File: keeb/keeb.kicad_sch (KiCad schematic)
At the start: 162 parts, among them J101 AVR-ISP-6, J102 USB_C_Receptacle_USB2.0, SW101 SW_Push, SW102 SW_Push, SW103 SW_Push, SW104 SW_Push, SW105 SW_Push, SW106 SW_Push, SW107 SW_Push, SW108 SW_Push, SW109 SW_Push, SW110 SW_Push, SW111 SW_Push, SW112 SW_Push, SW113 SW_Push, SW114 SW_Push, SW115 SW_Push, SW116 SW_Push, SW117 SW_Push, SW118 SW_Push, SW119 SW_Push, SW120 SW_Push, SW121 SW_Push, SW122 SW_Push, SW123 SW_Push, SW124 SW_Push, SW125 SW_Push, SW126 SW_Push, SW127 SW_Push, SW128 SW_Push, SW129 SW_Push, SW130 SW_Push, SW131 SW_Push, SW132 SW_Push, SW133 SW_Push, SW134 SW_Push, SW135 SW_Push, SW136 SW_Push, SW137 SW_Push, SW138 SW_Push, SW139 SW_Push, SW140 SW_Push, SW141 SW_Push, SW142 SW_Push, SW143 SW_Push, SW144 SW_Push, SW145 SW_Push, SW146 SW_Push, SW147 SW_Push, SW148 SW_Push, SW149 SW_Push, SW150 SW_Push, SW151 SW_Push, SW152 SW_Push, SW153 SW_Push, SW154 SW_Push, SW155 SW_Push, SW156 SW_Push, SW157 SW_Push, SW158 SW_Push, SW159 SW_Push, SW160 SW_Push, SW161 SW_Push, SW162 SW_Push, SW163 SW_Push, SW164 SW_Push, SW165 SW_Push, SW166 SW_Push, SW167 SW_Push, U101 TPD2S017, U102 ATmega32U4-MU, Y101 16Mhz

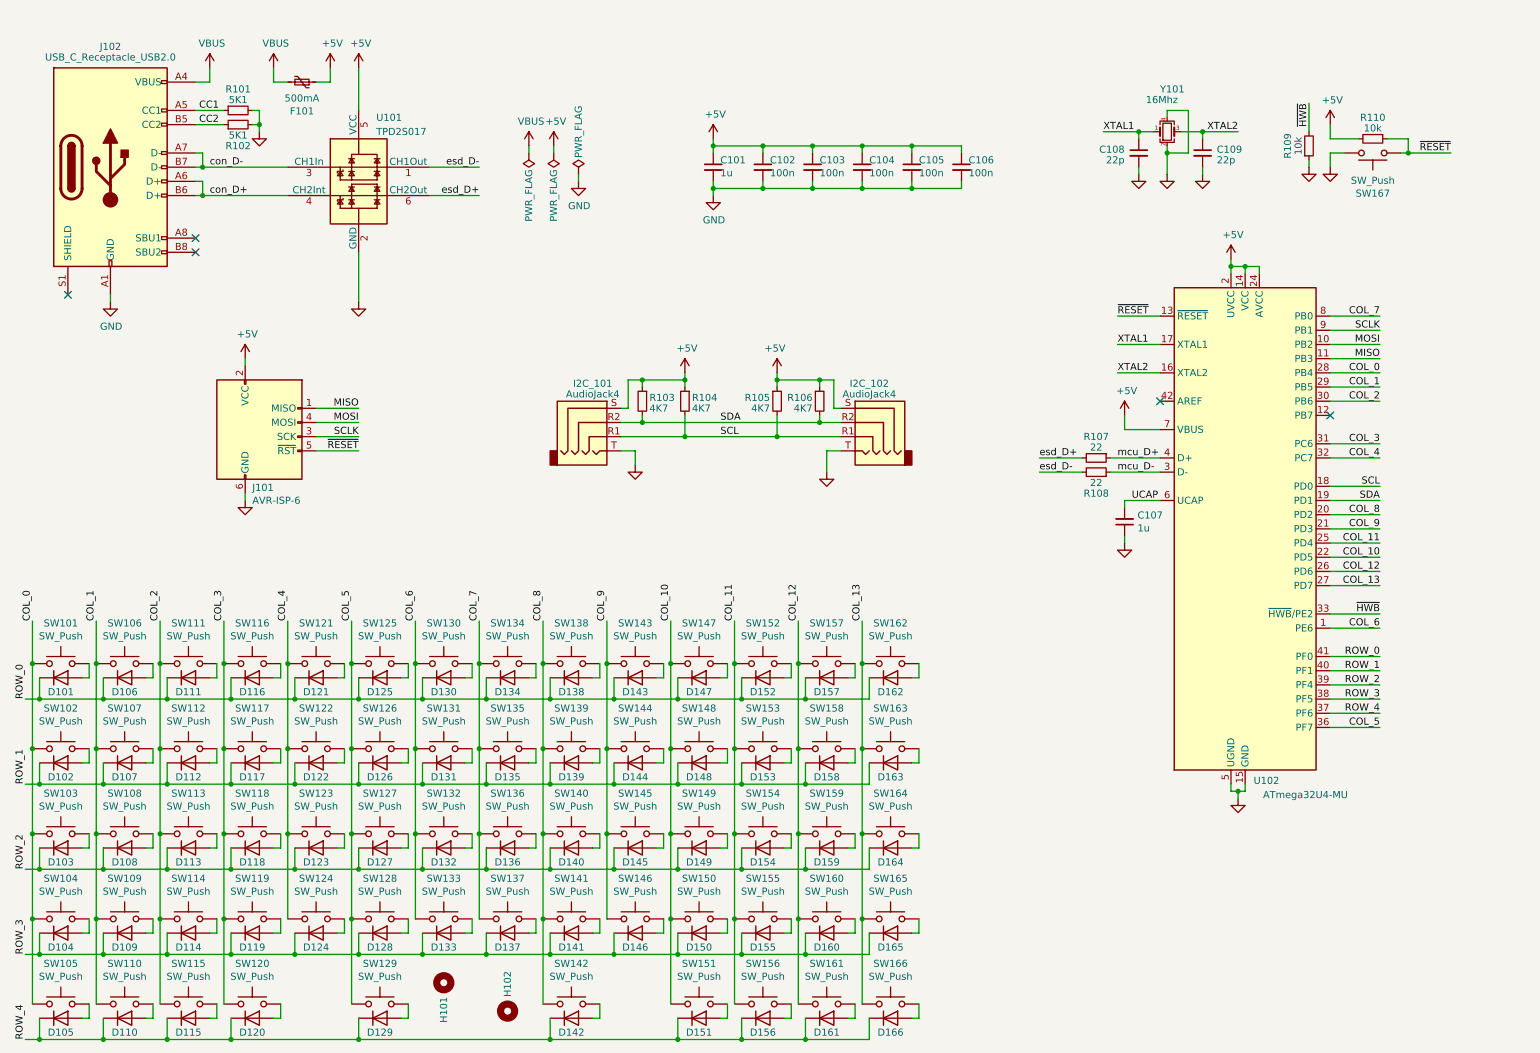
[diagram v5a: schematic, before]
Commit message: HTML Bom, osc load cap redo and schem org
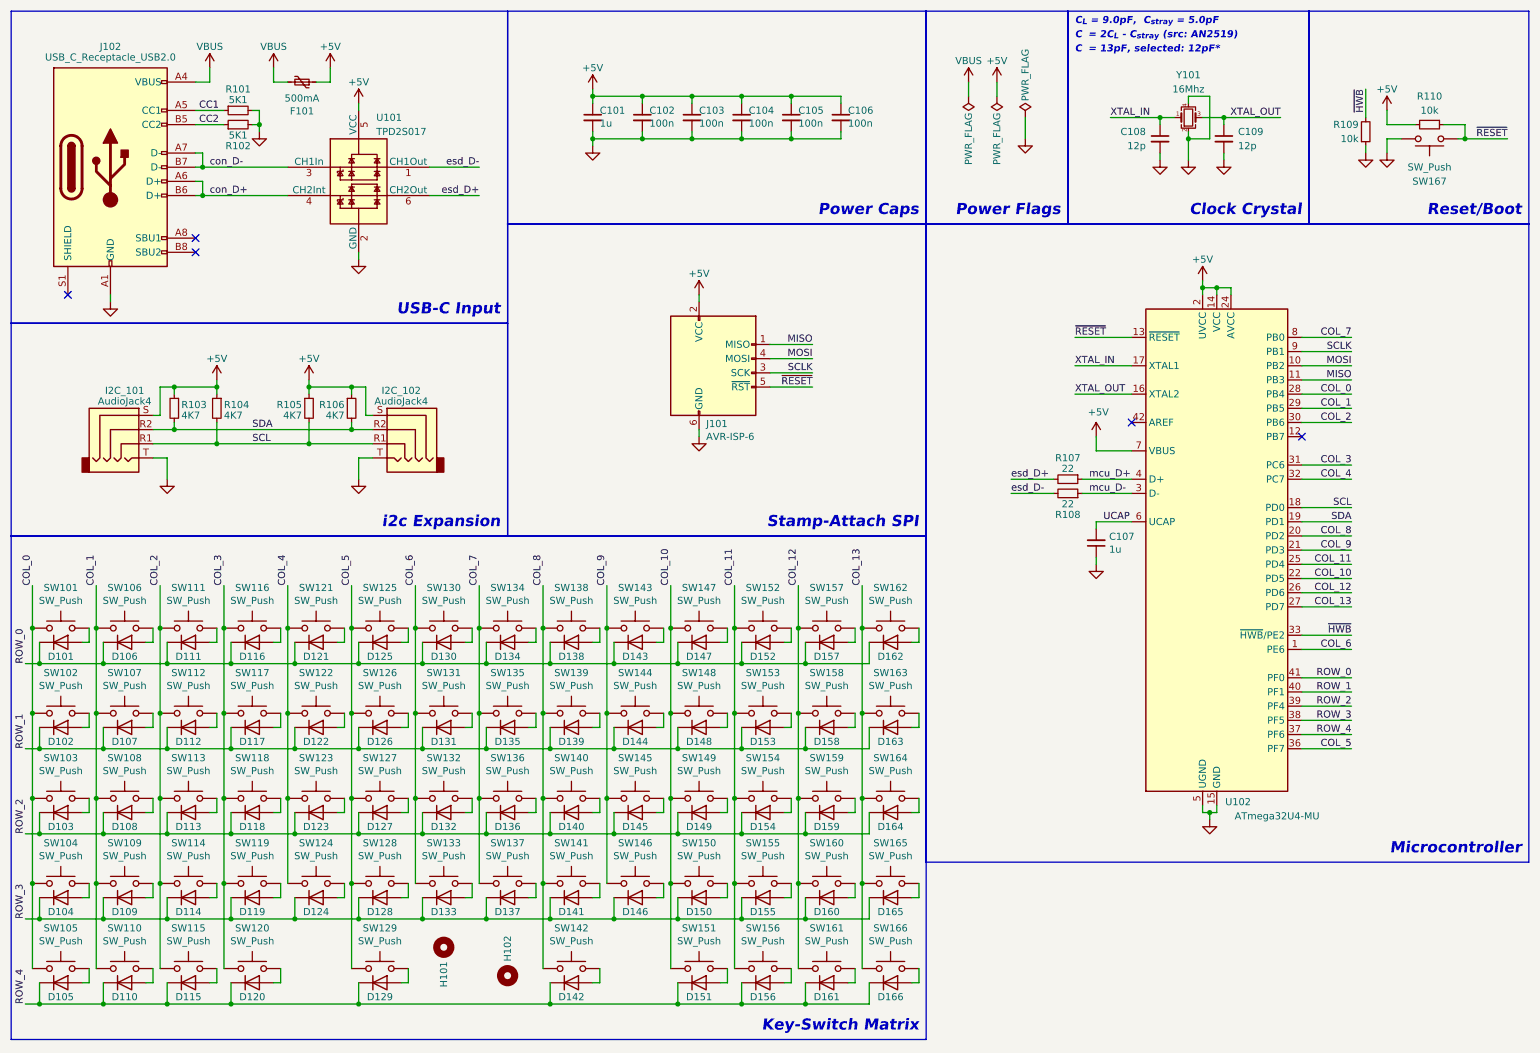
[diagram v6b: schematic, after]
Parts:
- C108, C109: value 22p -> 12p; LCSC # C1555 -> C1547; LCSC Link https://www.lcsc.com/product-detail/Multilayer-Ceramic-Capacitors-MLCC---SMD-SMT_FH-Guangdong-Fenghua-Advanced-Tech-FH-Guangdong-Fenghua-Advanced-Tech-0402CG220J500NT_C1555.html -> https://www.lcsc.com/product-detail/Multilayer-Ceramic-Capacitors-MLCC---SMD-SMT_FH-Guangdong-Fenghua-Advanced-Tech-FH-Guangdong-Fenghua-Advanced-Tech-0402CG120J500NT_C1547.html
- I2C_101, I2C_102: symbol Connector:AudioJack4 -> Connector_Audio:AudioJack4
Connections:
- net XTAL1 renamed XTAL_IN
- net XTAL2 renamed XTAL_OUT
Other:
- note added: "C_{ } = 13pF, selected: 12pF*"
- note added: "C_{ } = 2C_{L} - C_{stray} (src: AN2519)"
- note added: "C_{L} = 9.0pF, C_{stray} = 5.0pF"
- note added: "Clock Crystal"
- note added: "Key-Switch Matrix"
- note added: "Microcontroller"
- note added: "Power Caps"
- note added: "Power Flags"
- note added: "Reset/Boot"
- note added: "Stamp-Attach SPI"
- note added: "USB-C Input"
- note added: "i2c Expansion"
- moved on the sheet: C101, C102, C103, C104, C105, C106, C107, C108, C109, D101, D102, D103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
